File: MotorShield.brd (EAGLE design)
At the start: 85 x 56 mm, 88 parts, among them IC1 OPA4340E, IC2 OPA4340E

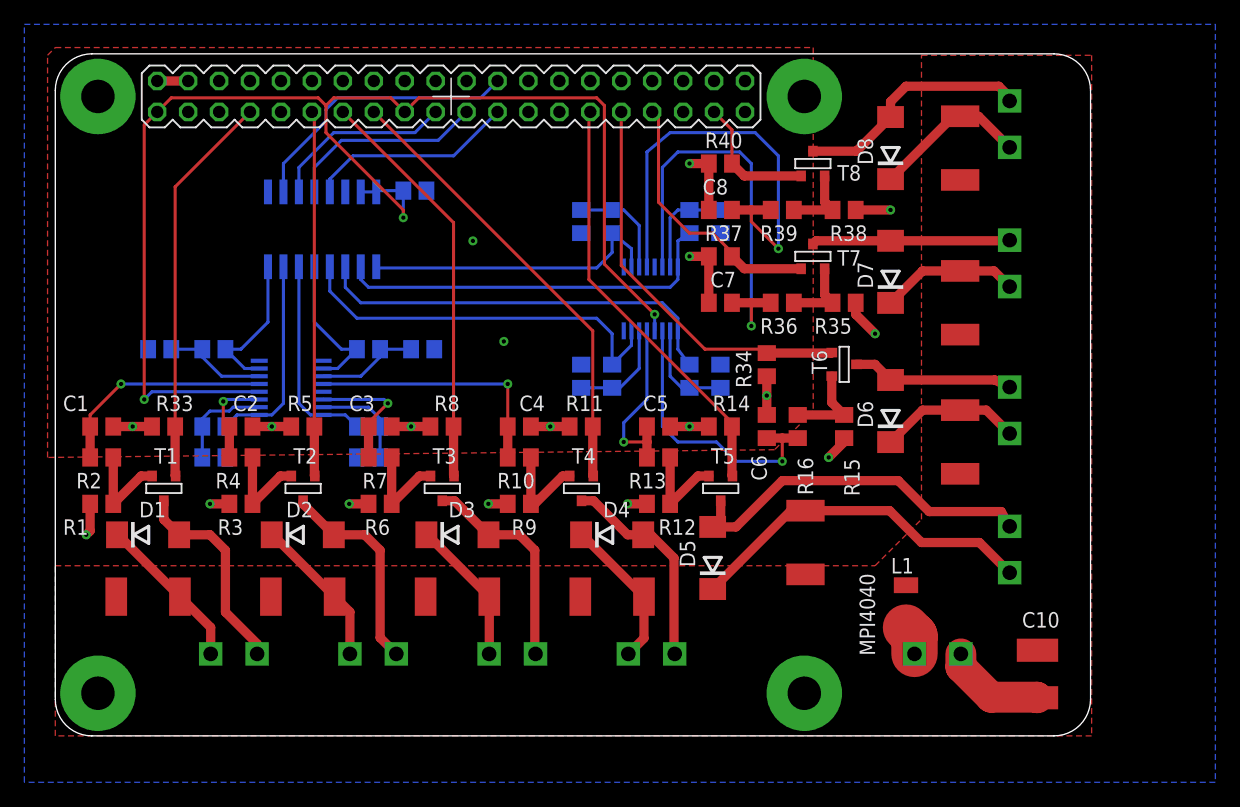
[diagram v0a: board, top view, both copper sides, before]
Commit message: named connector blocks and ADC
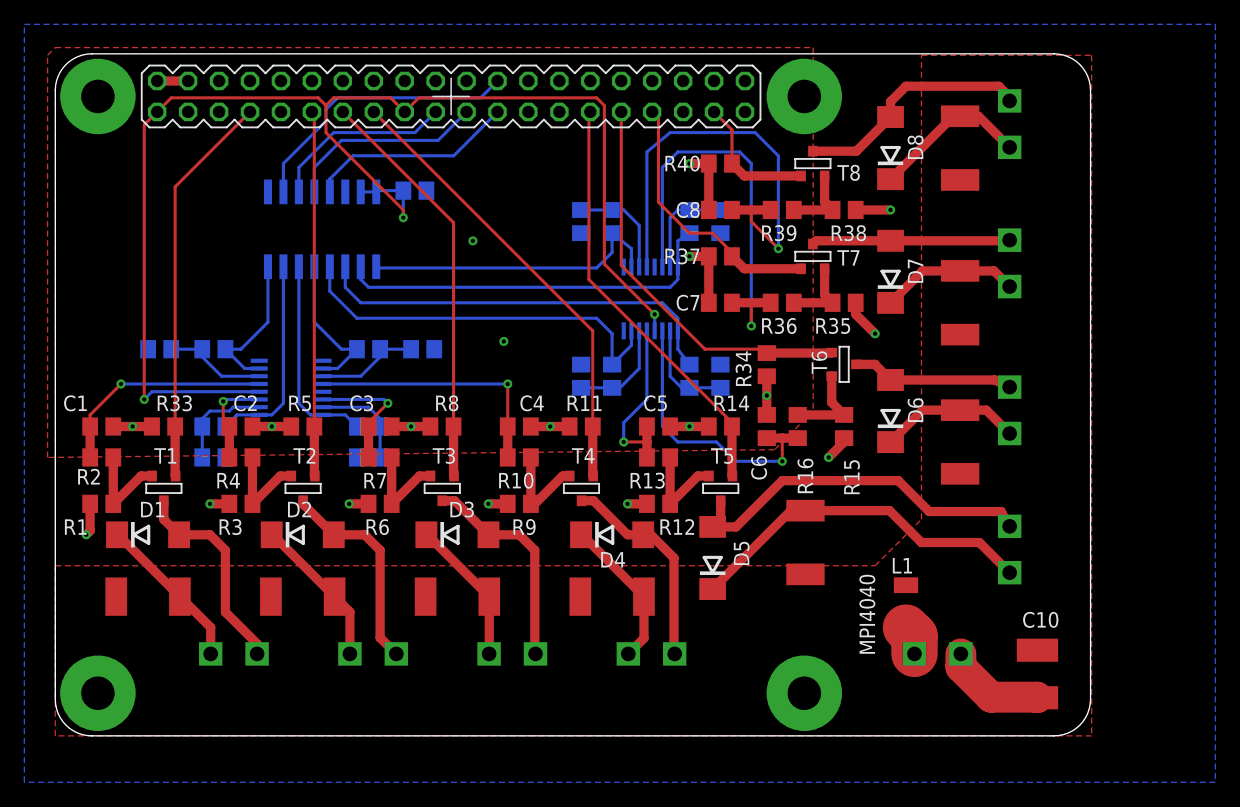
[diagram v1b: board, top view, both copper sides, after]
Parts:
- renumbered U$1 to X2, U$16 to X9, U$2 to X3, U$3 to X4, U$34 to X1, U$4 to X5, U$5 to X, U$58 to IC3, U$6 to X7, U$7 to X8

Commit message: added LEDs that signalize active output to close IUNO-TDM/MotorShield#6
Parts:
- added LED1, LED2, LED3, LED4, LED5, LED6, LED7, LED8: yellow, led:CHIP-LED0603
- added R41, R42, R43, R44, R45, R46, R47, R48: 2k2, rcl:R0603
- moved F1 4.13 mm to (11.7, 11.4)
- moved F2 2.86 mm to (23.2, 11.4)
- moved D2 2.22 mm to (22.5, 16.5)
- moved F5 1.59 mm to (61.6, 14.3), turned to 0 degrees
- moved F3 1.59 mm to (34.6, 11.4)
- moved R35 1.42 mm to (63.5, 34.9), turned to 90 degrees
- moved D5 1.27 mm to (55.2, 14.6)
- moved F8 0.95 mm to (74.3, 47.3)
- moved F4 0.32 mm to (46.0, 11.4)
- moved F6 0.32 mm to (74.3, 23.8)
- moved F7 0.32 mm to (74.3, 35.9)
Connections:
- new net N$16: LED1.A, R41.1
- new net N$19: LED2.A, R42.1
- new net N$20: LED3.A, R43.1
- new net N$21: LED5.A, R45.1
- new net N$23: LED4.A, R44.1
- new net N$24: LED6.A, R46.1
- new net N$25: LED7.A, R47.1
- new net N$30: LED8.A, R48.1
- net 24V/1A: now also R41.2
- net N$10: now also LED2.C
- net N$12: now also R43.2
- net N$13: now also R42.2
- net N$17: now also LED3.C
- net N$2: now also LED1.C
- net N$26: now also LED4.C
- net N$38: now also LED5.C
- net N$4: now also R48.2
- net N$45: now also LED6.C
- net N$5: now also R47.2
- net N$51: now also LED7.C
- net N$57: now also LED8.C
- net N$7: now also R46.2
- net N$8: now also R45.2
- net N$9: now also R44.2
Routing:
- net 24V/1A: track 13.0 -> 20.7 mm
- net N$12: track 12.0 -> 18.4 mm
- net N$13: track 12.5 -> 17.3 mm
- net N$9: track 12.5 -> 17.2 mm
- net N$2: track 17.2 -> 21.5 mm
- net N$30: track 0.00 -> 3.95 mm
- net N$10: track 17.2 -> 20.7 mm
- net N$25: track 0.00 -> 3.42 mm
- net N$24: track 0.00 -> 3.42 mm
- net N$51: track 16.4 -> 19.7 mm
- net N$26: track 17.4 -> 20.7 mm
- net N$45: track 13.2 -> 16.4 mm
- net N$17: track 17.8 -> 20.4 mm
- net N$21: track 0.00 -> 1.89 mm
- net GND: track 55.5 -> 54.2 mm
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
